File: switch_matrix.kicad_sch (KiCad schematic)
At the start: 8 parts, among them SW1 MX_SW_solder, SW2 MX_SW_solder, SW3 MX_SW_solder, SW4 MX_SW_solder

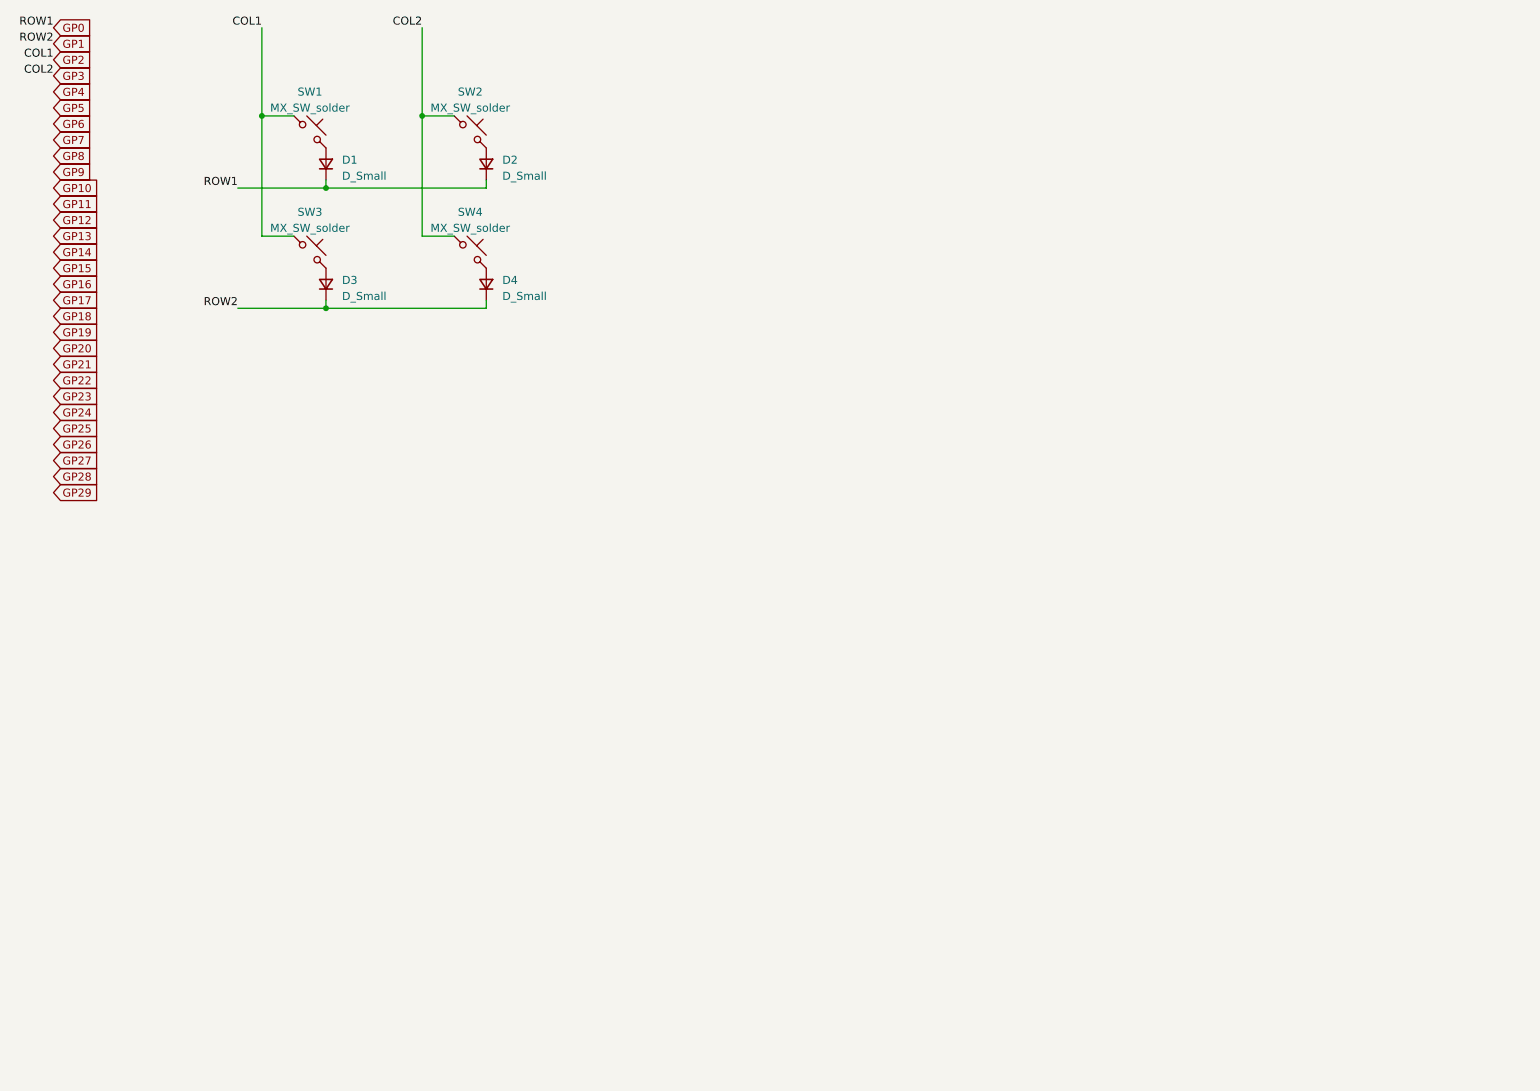
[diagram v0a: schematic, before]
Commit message: Update Schematic with keyboard layout
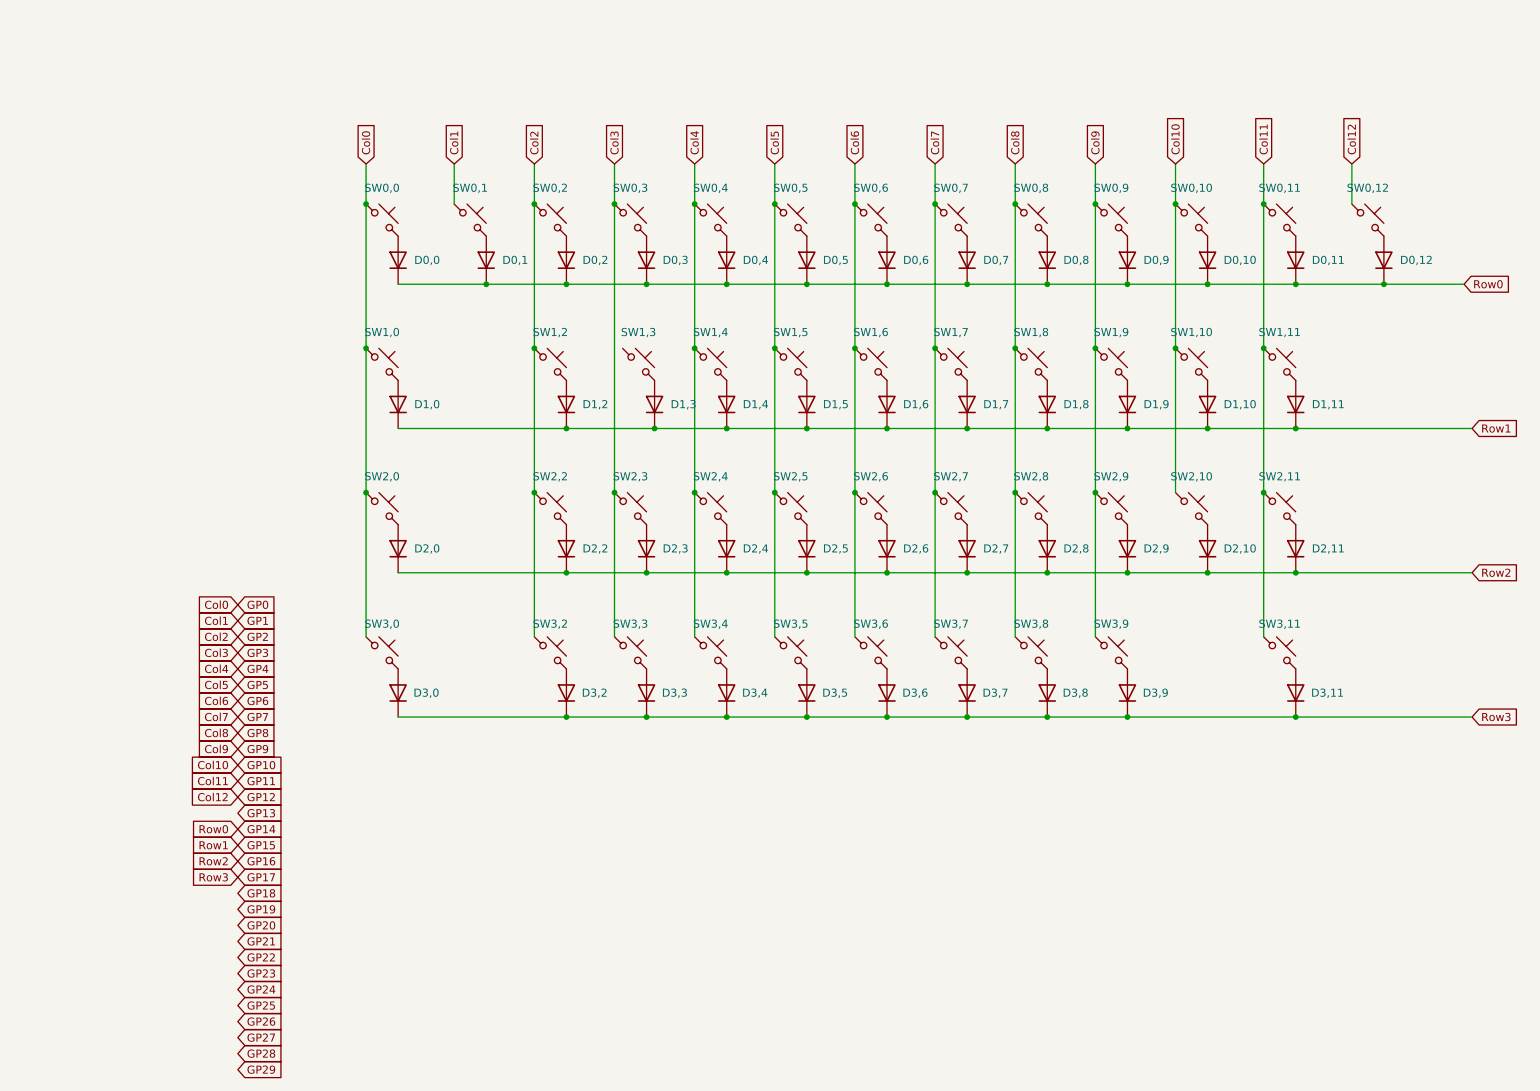
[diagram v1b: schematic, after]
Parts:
- removed D1, D2, D3, D4: D_Small, Diode_SMD:D_SOD-123, symbol Device:D_Small
- removed SW1, SW2, SW3, SW4: MX_SW_solder, marbastlib-mx:SW_MX_1u, symbol marbastlib-mx:MX_SW_solder
- added D0,0, D0,1, D0,10, D0,11, D0,12, D0,2, D0,3, D0,4, D0,5, D0,6, D0,7, D0,8, D0,9, D1,0, D1,10, D1,11, D1,2, D1,3, D1,4, D1,5, D1,6, D1,7, D1,8, D1,9, D2,0, D2,10, D2,11, D2,2, D2,3, D2,4, D2,5, D2,6, D2,7, D2,8, D2,9, D3,0, D3,11, D3,2, D3,3, D3,4, D3,5, D3,6, D3,7, D3,8, D3,9: 1N4148W, Diode_SMD:D_SOD-123, symbol Diode:1N4148W
- added SW0,0, SW0,1, SW0,10, SW0,11, SW0,2, SW0,3, SW0,4, SW0,5, SW0,6, SW0,7, SW0,8, SW0,9, SW1,10, SW1,2, SW1,3, SW1,4, SW1,5, SW1,6, SW1,7, SW1,8, SW1,9, SW2,10, SW2,2, SW2,3, SW2,4, SW2,5, SW2,6, SW2,7, SW2,8, SW2,9, SW3,0, SW3,11, SW3,2, SW3,3, SW3,6: MX_SW_solder, PCM_marbastlib-mx:SW_MX_1u, symbol PCM_marbastlib-mx:MX_SW_solder
- added SW0,12, SW2,0: MX_SW_solder, PCM_marbastlib-mx:SW_MX_1.5u, symbol PCM_marbastlib-mx:MX_SW_solder
- added SW1,0: MX_SW_solder, PCM_marbastlib-mx:SW_MX_1.75u, symbol PCM_marbastlib-mx:MX_SW_solder
- added SW1,11: MX_SW_solder, PCM_marbastlib-mx:STAB_MX_P_2.25u, symbol PCM_marbastlib-mx:MX_SW_solder
- added SW2,11: MX_SW_solder, PCM_marbastlib-mx:STAB_MX_P_2u, symbol PCM_marbastlib-mx:MX_SW_solder
- added SW3,4, SW3,7, SW3,8, SW3,9: MX_SW_solder, PCM_marbastlib-mx:SW_MX_1.25u, symbol PCM_marbastlib-mx:MX_SW_solder
- added SW3,5: MX_SW_solder, PCM_marbastlib-mx:STAB_MX_P_3u, symbol PCM_marbastlib-mx:MX_SW_solder
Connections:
- net GP14: now also D0,0.1 (K), D0,1.1 (K), D0,10.1 (K), D0,11.1 (K), D0,12.1 (K), D0,2.1 (K), D0,3.1 (K), D0,4.1 (K), D0,5.1 (K), D0,6.1 (K), D0,7.1 (K), D0,8.1 (K), D0,9.1 (K)
- net GP15: now also D1,0.1 (K), D1,10.1 (K), D1,11.1 (K), D1,2.1 (K), D1,3.1 (K), D1,4.1 (K), D1,5.1 (K), D1,6.1 (K), D1,7.1 (K), D1,8.1 (K), D1,9.1 (K)
- net GP16: now also D2,0.1 (K), D2,10.1 (K), D2,11.1 (K), D2,2.1 (K), D2,3.1 (K), D2,4.1 (K), D2,5.1 (K), D2,6.1 (K), D2,7.1 (K), D2,8.1 (K), D2,9.1 (K)
- net GP17: now also D3,0.1 (K), D3,11.1 (K), D3,2.1 (K), D3,3.1 (K), D3,4.1 (K), D3,5.1 (K), D3,6.1 (K), D3,7.1 (K), D3,8.1 (K), D3,9.1 (K)
- new net: D2,11.2 (A), SW2,11.2
- new net: D1,10.2 (A), SW1,10.2
- new net: D3,0.2 (A), SW3,0.2
- new net: D0,11.2 (A), SW0,11.2
- new net: D0,2.2 (A), SW0,2.2
- new net: D2,4.2 (A), SW2,4.2
- new net: D2,3.2 (A), SW2,3.2
- new net: D1,0.2 (A), SW1,0.2
- new net: D1,7.2 (A), SW1,7.2
- new net: D1,9.2 (A), SW1,9.2
- new net: D1,6.2 (A), SW1,6.2
- new net: D2,9.2 (A), SW2,9.2
- new net: D1,11.2 (A), SW1,11.2
- new net: D2,0.2 (A), SW2,0.2
- new net: D3,11.2 (A), SW3,11.2
- new net: D0,1.2 (A), SW0,1.2
- new net: D1,5.2 (A), SW1,5.2
- new net: D1,3.2 (A), SW1,3.2
- new net: D1,4.2 (A), SW1,4.2
- new net: D3,2.2 (A), SW3,2.2
- new net: D0,9.2 (A), SW0,9.2
- new net: D3,7.2 (A), SW3,7.2
- new net: D2,7.2 (A), SW2,7.2
- new net: D3,6.2 (A), SW3,6.2
- new net: D2,10.2 (A), SW2,10.2
- new net: D3,8.2 (A), SW3,8.2
- new net: D2,6.2 (A), SW2,6.2
- new net: D3,5.2 (A), SW3,5.2
- new net: D0,8.2 (A), SW0,8.2
- new net: D0,10.2 (A), SW0,10.2
- new net: D0,3.2 (A), SW0,3.2
- new net: D3,3.2 (A), SW3,3.2
- new net: D0,12.2 (A), SW0,12.2
- new net: D2,2.2 (A), SW2,2.2
- new net: D0,7.2 (A), SW0,7.2
- new net: D1,8.2 (A), SW1,8.2
- new net: D2,5.2 (A), SW2,5.2
- new net: D0,4.2 (A), SW0,4.2
- new net: D2,8.2 (A), SW2,8.2
- new net: D1,2.2 (A), SW1,2.2
- new net: D3,9.2 (A), SW3,9.2
- new net: D0,5.2 (A), SW0,5.2
- new net: D3,4.2 (A), SW3,4.2
- new net: D0,6.2 (A), SW0,6.2
- new net: D0,0.2 (A), SW0,0.2
- new net Col0: SW0,0.1, SW1,0.1, SW2,0.1, SW3,0.1
- new net Col1: SW0,1.1
- new net Col10: SW0,10.1, SW1,10.1, SW2,10.1
- new net Col11: SW0,11.1, SW1,11.1, SW2,11.1, SW3,11.1
- new net Col12: SW0,12.1
- new net Col2: SW0,2.1, SW1,2.1, SW2,2.1, SW3,2.1
- new net Col3: SW0,3.1, SW2,3.1, SW3,3.1
- new net Col4: SW0,4.1, SW1,4.1, SW2,4.1, SW3,4.1
- new net Col5: SW0,5.1, SW1,5.1, SW2,5.1, SW3,5.1
- new net Col6: SW0,6.1, SW1,6.1, SW2,6.1, SW3,6.1
- new net Col7: SW0,7.1, SW1,7.1, SW2,7.1, SW3,7.1
- new net Col8: SW0,8.1, SW1,8.1, SW2,8.1, SW3,8.1
- new net Col9: SW0,9.1, SW1,9.1, SW2,9.1, SW3,9.1
